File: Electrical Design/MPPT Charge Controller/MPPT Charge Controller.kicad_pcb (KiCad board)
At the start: 4 copper layers, 32 x 80 mm, 72 parts, among them J1 Conn_01x02_Socket, J2 Conn_01x02_Socket, J3 Conn_01x02_Socket, Q1 Q_Dual_NMOS_S1G1S2G2D2D2D1D1, Q2 Q_Dual_NMOS_S1G1S2G2D2D2D1D1, Q3 2N7002, U2 AP63203WU, U3 ACS712xLCTR-05B, U4 ACS712

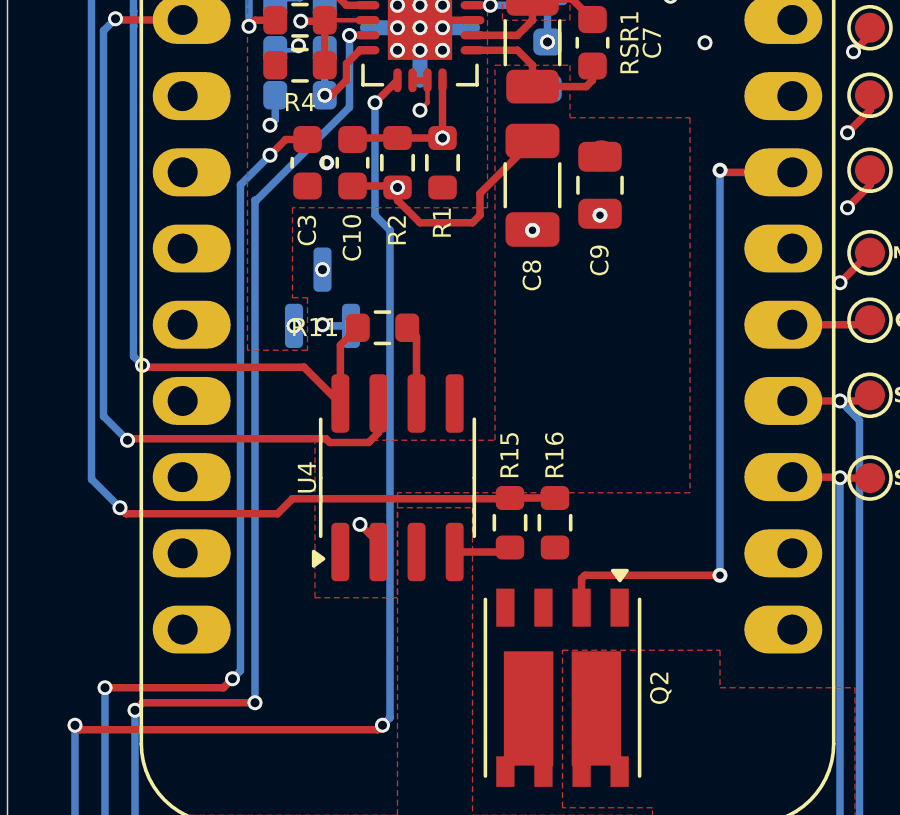
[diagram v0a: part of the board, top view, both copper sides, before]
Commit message: fixed R4 inconsistency
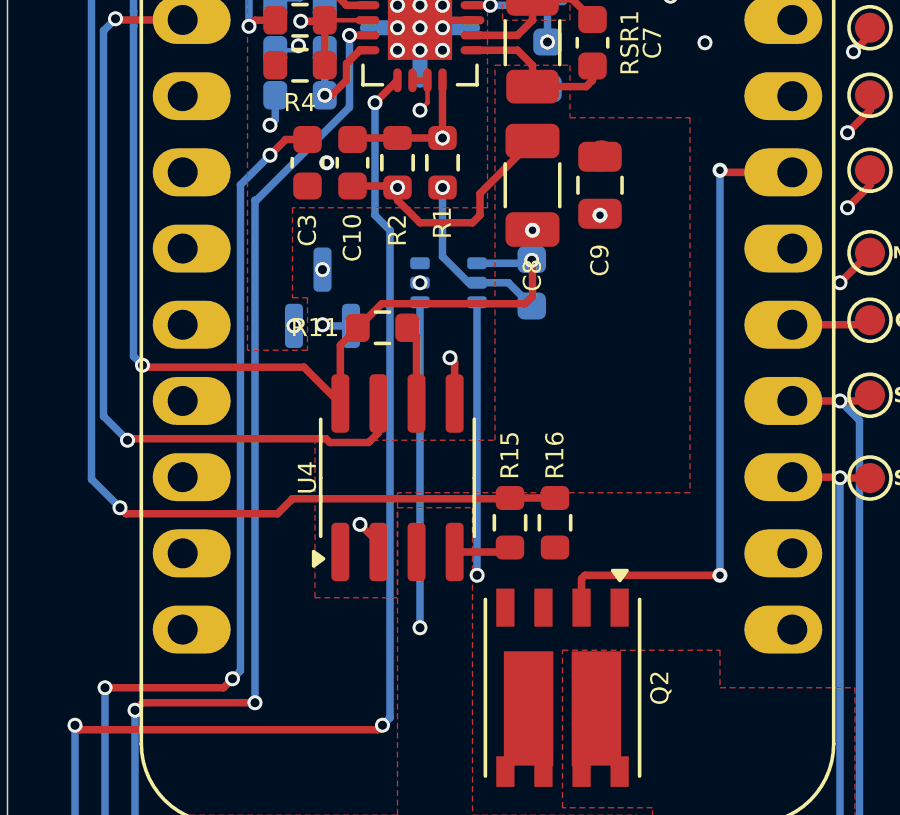
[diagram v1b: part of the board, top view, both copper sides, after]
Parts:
- added C15: 0.1uF, Capacitor_SMD:C_0603_1608Metric, B.Cu at (111.5, 107.5)
- added U5: MCP4018, Package_TO_SOT_SMD:SOT-363_SC-70-6, B.Cu at (108.7, 107.5)
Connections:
- A1 pad 17: unconnected-(A1-SDA/IO23-Pad17) -> /SDA
- A1 pad 18: unconnected-(A1-SCL/IO22-Pad18) -> /SCL
- Q2 pad 6: unconnected-(Q2B-D-Pad6) -> unconnected-(Q2B-D-Pad5)
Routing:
- net /SDA: track 0.00 -> 23.3 mm, vias 0 -> 1
- net /SCL: track 0.00 -> 19.9 mm, vias 0 -> 1
- net +3.3V: track 74.2 -> 83.5 mm, vias 2 -> 3
- net PWR GND: track 2.94 -> 8.90 mm, vias 12 -> 13
- net GND: track 0.23 -> 1.82 mm, vias 8 -> 9
- net /MPPSET: vias 3 -> 4

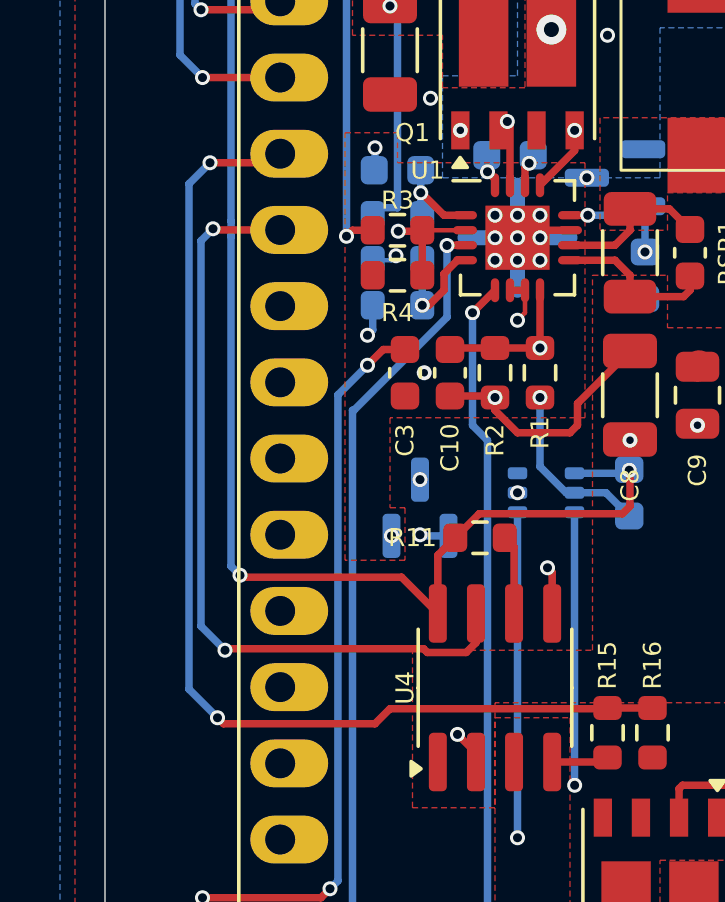
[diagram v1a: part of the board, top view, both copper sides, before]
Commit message: Added battery temp thermistor connector
Also cleaned up directory and added .gitignore
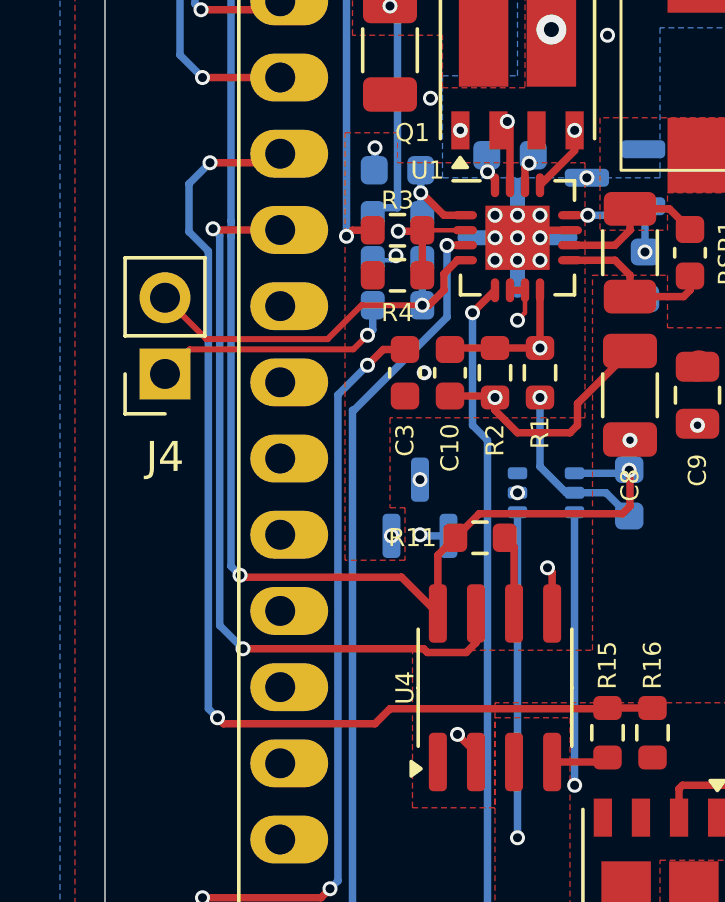
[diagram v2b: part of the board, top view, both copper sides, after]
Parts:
- added J4: ~, Connector_PinSocket_2.54mm:PinSocket_1x02_P2.54mm_Vertical, F.Cu at (96.0, 103.5)
- R13: value 68k -> 36k
- R16: value 150k -> 100k
- R4: value 36k -> DNP
- R7, R8: value 10k -> 100
- U3: value ACS712xLCTR-05B -> ACS712
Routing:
- net /TS: track 25.7 -> 35.3 mm
- net PWR GND: track 8.90 -> 16.2 mm
- net /Battery Current: track 26.4 -> 25.6 mm
